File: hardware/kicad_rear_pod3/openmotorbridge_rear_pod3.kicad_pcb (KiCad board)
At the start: 2 copper layers, 50 x 35 mm, 18 parts, among them J1 6-Pin_OMM_Female_Socket, U1 ESP32-C3-WROOM-02, U2 MAX-M10S_GNSS, U3 SX1262_LoRa_+22dBm, U4 DS2401_1Wire_ID

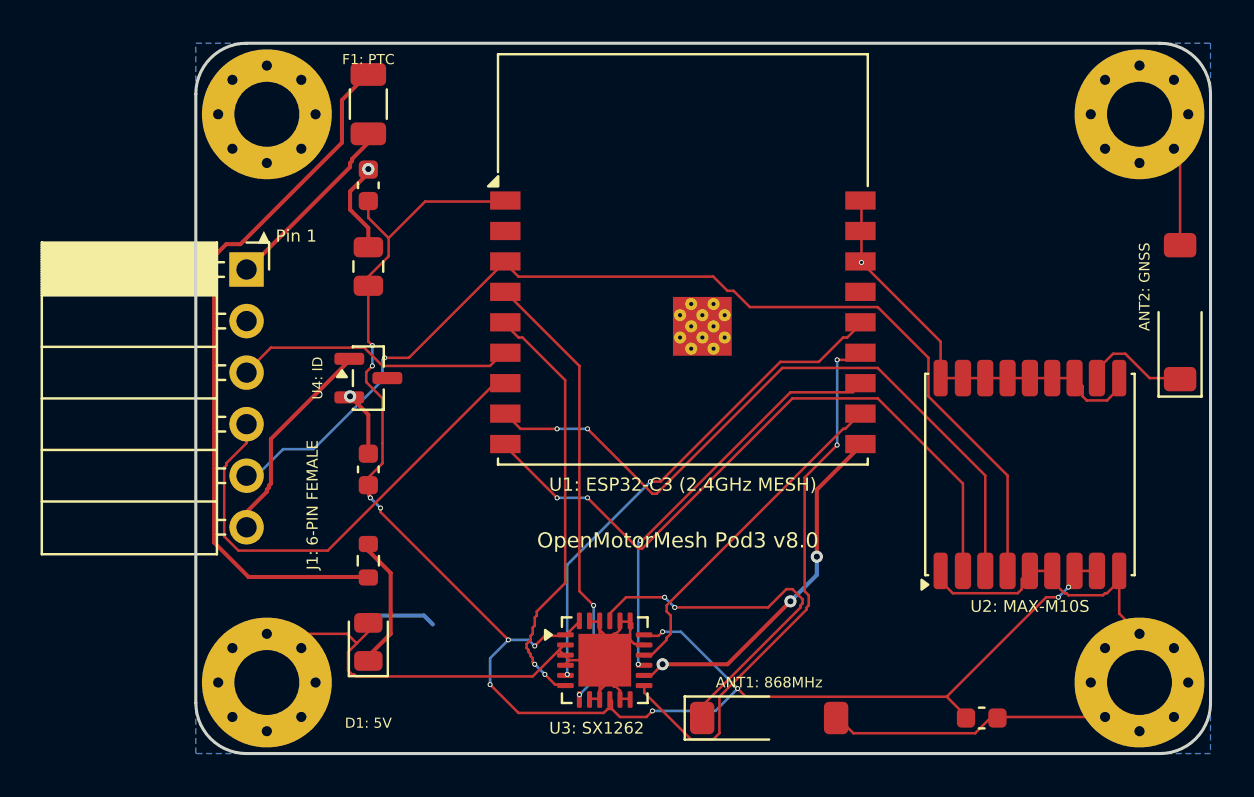
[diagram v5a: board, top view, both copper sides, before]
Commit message: Implement comprehensive JLCPCB PCB Design Verification Plan (ERC/DRC/DFM/DFA) and standardize all PCB layouts
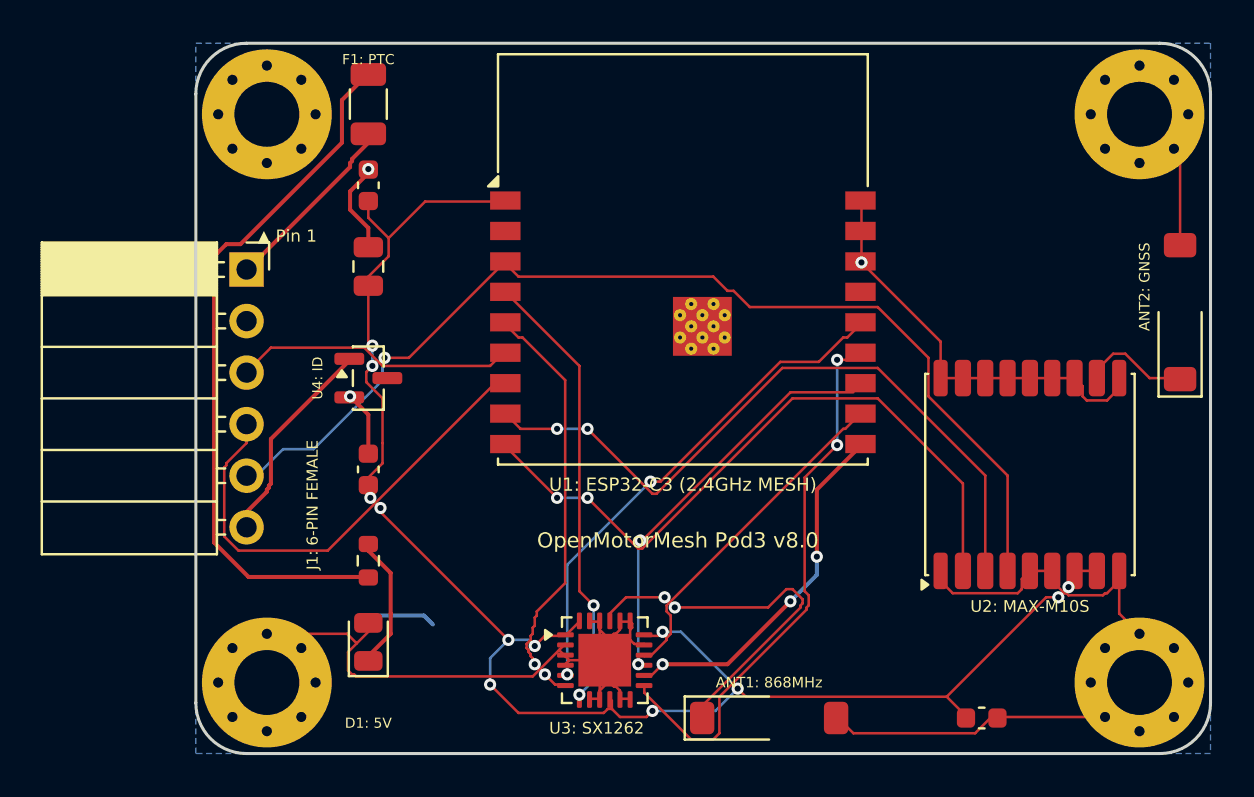
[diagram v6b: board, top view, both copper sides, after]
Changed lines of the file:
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@@
 	(via
 		(at 123 99)
-		(size 0.25)
-		(drill 0.15)
+		(size 0.6)
+		(drill 0.3)
 		(layers "F.Cu" "B.Cu")
 		(net "VCC_3V3")
@@
 	(via
 		(at 108.6 92.4)
-		(size 0.25)
-		(drill 0.15)
+		(size 0.6)
+		(drill 0.3)
 		(layers "F.Cu" "B.Cu")
 		(net "VCC_3V3")
@@
 	(via
 		(at 142.5 97.3)
-		(size 0.25)
-		(drill 0.15)
+		(size 0.6)
+		(drill 0.3)
 		(layers "F.Cu" "B.Cu")
 		(net "VCC_3V3")
@@
 	(via
 		(at 116.7 99.7)
-		(size 0.25)
-		(drill 0.15)
+		(size 0.6)
+		(drill 0.3)
 		(layers "F.Cu" "B.Cu")
 		(net "VCC_3V3")
@@
 	(via
 		(at 122.5 102.9)
-		(size 0.25)
-		(drill 0.15)
+		(size 0.6)
+		(drill 0.3)
 		(layers "F.Cu" "B.Cu")
 		(net "VCC_3V3")
@@
 	(via
 		(at 114.5 101.6)
-		(size 0.25)
-		(drill 0.15)
+		(size 0.6)
+		(drill 0.3)
 		(layers "F.Cu" "B.Cu")
 		(net "VCC_3V3")
@@
 	(via
 		(at 115.4 99.4)
-		(size 0.25)
-		(drill 0.15)
+		(size 0.6)
+		(drill 0.3)
 		(layers "F.Cu" "B.Cu")
 		(net "VCC_3V3")
@@
 	(via
 		(at 143 96.8)
-		(size 0.25)
-		(drill 0.15)
+		(size 0.6)
+		(drill 0.3)
 		(layers "F.Cu" "B.Cu")
 		(net "VCC_3V3")
@@
 	(via
 		(at 126.7 101.8)
-		(size 0.25)
-		(drill 0.15)
+		(size 0.6)
+		(drill 0.3)
 		(layers "F.Cu" "B.Cu")
 		(net "VCC_3V3")
@@
 	(via
 		(at 108.7 85.9)
-		(size 0.25)
-		(drill 0.15)
+		(size 0.6)
+		(drill 0.3)
 		(layers "F.Cu" "B.Cu")
 		(net "VCC_3V3")
@@
 	(via
 		(at 109.1 92.9)
-		(size 0.25)
-		(drill 0.15)
+		(size 0.6)
+		(drill 0.3)
 		(layers "F.Cu" "B.Cu")
 		(net "VCC_3V3")
@@
 	(via
 		(at 108.7 84.9)
-		(size 0.25)
-		(drill 0.15)
+		(size 0.6)
+		(drill 0.3)
 		(layers "F.Cu" "B.Cu")
 		(net "VCC_3V3")
@@
 	(via
 		(at 132.8 80.8)
-		(size 0.25)
-		(drill 0.15)
+		(size 0.6)
+		(drill 0.3)
 		(layers "F.Cu" "B.Cu")
 		(net "GND")
@@
 	(via
 		(at 109.3 85.5)
-		(size 0.25)
-		(drill 0.15)
+		(size 0.6)
+		(drill 0.3)
 		(layers "F.Cu" "B.Cu")
 		(net "GNSS_1PPS")
@@
 	(via
 		(at 122.4 91.6)
-		(size 0.25)
-		(drill 0.15)
+		(size 0.6)
+		(drill 0.3)
 		(layers "F.Cu" "B.Cu")
 		(net "LORA_NRST")
@@
 	(via
 		(at 118.3 101.1)
-		(size 0.25)
-		(drill 0.15)
+		(size 0.6)
+		(drill 0.3)
 		(layers "F.Cu" "B.Cu")
 		(net "LORA_NRST")
@@
 	(via
 		(at 117.2 101.1)
-		(size 0.25)
-		(drill 0.15)
+		(size 0.6)
+		(drill 0.3)
 		(layers "F.Cu" "B.Cu")
 		(net "LORA_BUSY")
@@
 	(via
 		(at 116.7 100.6)
-		(size 0.25)
-		(drill 0.15)
+		(size 0.6)
+		(drill 0.3)
 		(layers "F.Cu" "B.Cu")
 		(net "LORA_BUSY")
@@
 	(via
 		(at 118.9 102.1)
-		(size 0.25)
-		(drill 0.15)
+		(size 0.6)
+		(drill 0.3)
 		(layers "F.Cu" "B.Cu")
 		(net "LORA_DIO1")
@@
 	(via
 		(at 119.6 97.7)
-		(size 0.25)
-		(drill 0.15)
+		(size 0.6)
+		(drill 0.3)
 		(layers "F.Cu" "B.Cu")
 		(net "LORA_DIO1")
@@
 	(via
 		(at 131.6 89.8)
-		(size 0.25)
-		(drill 0.15)
+		(size 0.6)
+		(drill 0.3)
 		(layers "F.Cu" "B.Cu")
 		(net "LORA_NSS")
@@
 	(via
 		(at 131.6 85.6)
-		(size 0.25)
-		(drill 0.15)
+		(size 0.6)
+		(drill 0.3)
 		(layers "F.Cu" "B.Cu")
 		(net "LORA_NSS")
@@
 	(via
 		(at 121.9 94.5)
-		(size 0.25)
-		(drill 0.15)
+		(size 0.6)
+		(drill 0.3)
 		(layers "F.Cu" "B.Cu")
 		(net "LORA_MOSI")
@@
 	(via
 		(at 121.8 100.6)
-		(size 0.25)
-		(drill 0.15)
+		(size 0.6)
+		(drill 0.3)
 		(layers "F.Cu" "B.Cu")
 		(net "LORA_MOSI")
@@
 	(via
 		(at 123.1 97.3)
-		(size 0.25)
-		(drill 0.15)
+		(size 0.6)
+		(drill 0.3)
 		(layers "F.Cu" "B.Cu")
 		(net "LORA_ANT")
@@
 	(via
 		(at 123.6 97.8)
-		(size 0.25)
-		(drill 0.15)
+		(size 0.6)
+		(drill 0.3)
 		(layers "F.Cu" "B.Cu")
 		(net "LORA_ANT")
@@
 	(via
 		(at 117.8 89)
-		(size 0.25)
-		(drill 0.15)
+		(size 0.6)
+		(drill 0.3)
 		(layers "F.Cu" "B.Cu")
 		(net "GNSS_RXD")
@@
 	(via
 		(at 119.3 89)
-		(size 0.25)
-		(drill 0.15)
+		(size 0.6)
+		(drill 0.3)
 		(layers "F.Cu" "B.Cu")
 		(net "GNSS_RXD")
@@
 	(via
 		(at 117.8 92.4)
-		(size 0.25)
-		(drill 0.15)
+		(size 0.6)
+		(drill 0.3)
 		(layers "F.Cu" "B.Cu")
 		(net "GNSS_TXD")
@@
 	(via
 		(at 119.3 92.4)
-		(size 0.25)
-		(drill 0.15)
+		(size 0.6)
+		(drill 0.3)
 		(layers "F.Cu" "B.Cu")
 		(net "GNSS_TXD")

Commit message: Clean dangling stubs on Rear Pod 3 D1 GND and Pod Cartridge D+ audio traces, update 3D renders
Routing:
- net LORA_MOSI: track 20.1 -> 17.0 mm
- net GND: track 101.9 -> 101.1 mm
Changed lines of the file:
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@@
+	)
+	(segment
+		(start 108.5 98.56)
+		(end 107.5 98.56)
+		(width 0.25)
+		(layer "F.Cu")
+		(net "GND")
 	)
 	(segment
@@
 		(end 120.15 100.4)
 		(width 0.127)
+		(layer "F.Cu")
+		(net "GND")
+	)
+	(segment
+		(start 107.5 98.56)
+		(end 107.5 100)
+		(width 0.25)
 		(layer "F.Cu")
 		(net "GND")
@@
 		(drill 0.3)
 		(layers "F.Cu" "B.Cu")
-		(net "GND")
-	)
-	(segment
-		(start 111.68 98.64)
-		(end 111.24 98.2)
-		(width 0.2)
-		(layer "B.Cu")
-		(net "GND")
-	)
-	(segment
-		(start 111.24 98.2)
-		(end 108.7 98.2)
-		(width 0.2)
-		(layer "B.Cu")
-		(net "GND")
-	)
-	(segment
-		(start 108.48 76.24)
-		(end 108.5 76.2)
-		(width 0.2)
-		(layer "B.Cu")
-		(net "GND")
-	)
-	(segment
-		(start 107.6 87.44)
-		(end 107.6 87.4)
-		(width 0.2)
-		(layer "B.Cu")
 		(net "GND")
 	)
@@
 		(width 0.127)
 		(layer "F.Cu")
-		(net "LORA_MOSI")
-	)
-	(segment
-		(start 132.4 87.2)
-		(end 129.3 87.2)
-		(width 0.127)
-		(layer "F.Cu")

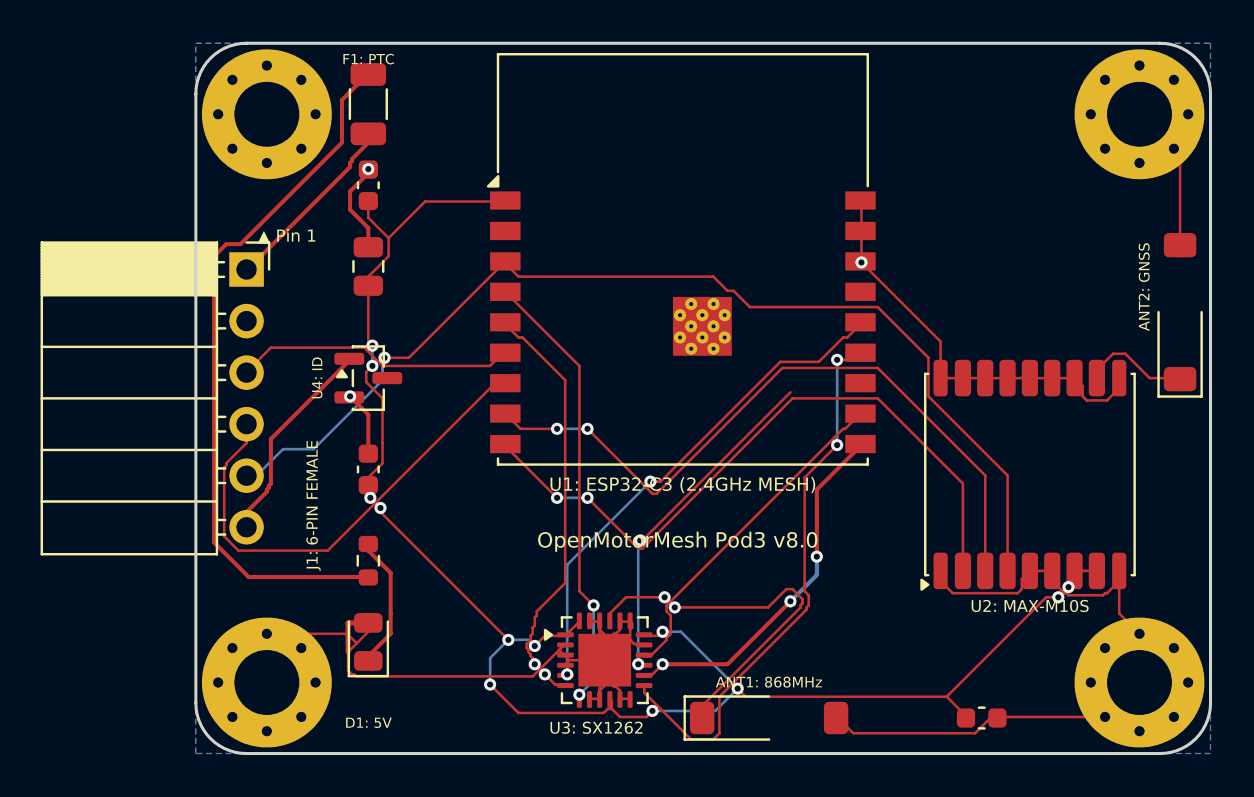
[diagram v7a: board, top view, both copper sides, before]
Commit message: feat(hardware): finalize JLCPCB-compliant autorouting across all 4 PCBs
- Configure JLCPCB standard net classes ('Default' & 'Power') in .kicad_pro and .kicad_pcb
- Set board setup constraints: 0.15/0.20mm trace, 0.60/0.30mm via, 0.127/0.15mm clearance
- Complete 100% autorouting for Main Board, Pod Base, Pod Cartridge, and Rear Pod 3
- Eliminate manual 2D trace generation scripts and planar crossing errors
- Update verification tool (verify_pcb_designs_jlcpcb.py) to audit 2-layer and 4-layer capabilities
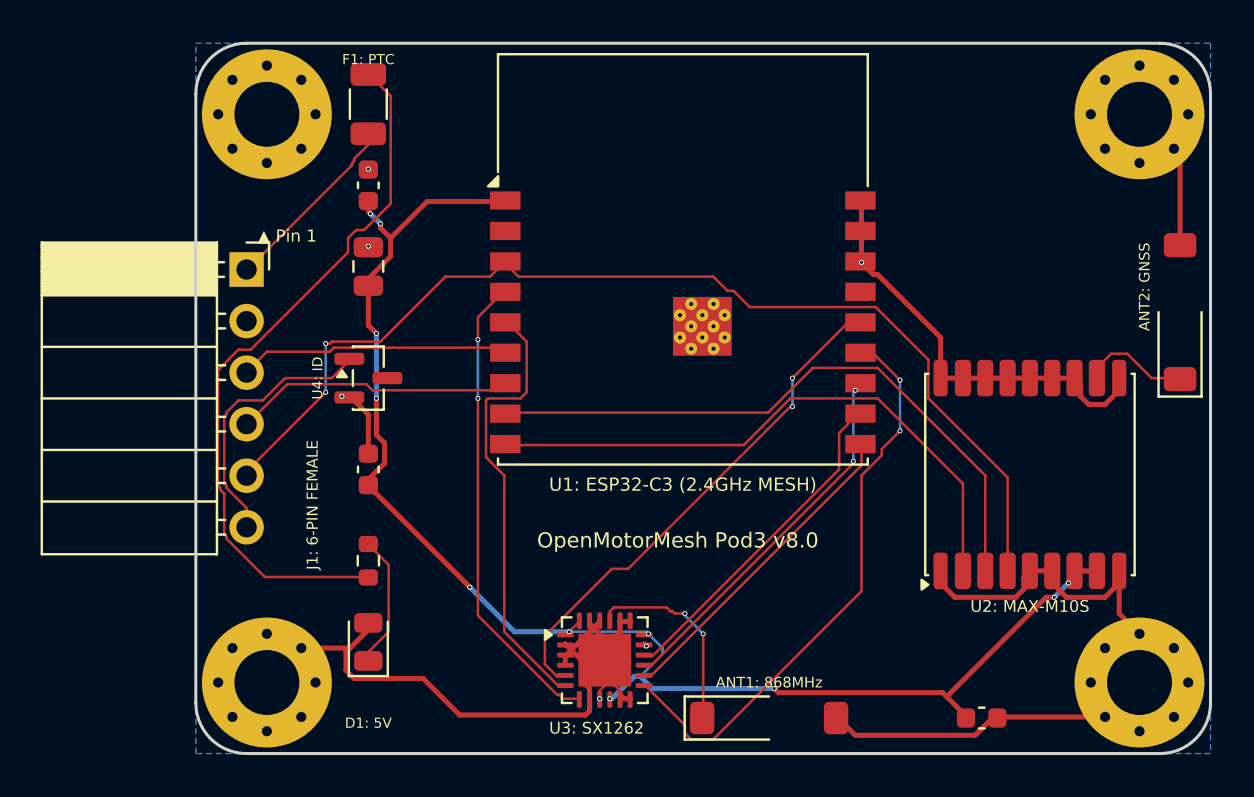
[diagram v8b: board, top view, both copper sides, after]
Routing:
- net GND: track 101.1 -> 90.7 mm, vias 3 -> 6
- net POD3_UART_RX: track 23.5 -> 13.8 mm
- net VCC_3V3: track 82.4 -> 73.0 mm, vias 12 -> 11
- net LORA_ANT: track 19.0 -> 9.99 mm
- net GNSS_TXD: track 33.9 -> 29.7 mm, vias 2 -> 0
- net GNSS_RXD: track 34.9 -> 31.6 mm, vias 2 -> 0
- net POD3_1WIRE_ID: track 10.4 -> 13.3 mm
- net LORA_SCK: track 17.9 -> 16.1 mm, vias 3 -> 0
- net LORA_MOSI: track 17.0 -> 18.6 mm
- net LORA_NSS: track 27.6 -> 28.9 mm
- net LORA_DIO1: track 22.3 -> 23.3 mm
- net LORA_BUSY: track 21.1 -> 22.1 mm, vias 2 -> 0
- net GNSS_1PPS: track 52.7 -> 53.3 mm, vias 1 -> 2
- net POD3_UART_TX: track 13.9 -> 13.4 mm
